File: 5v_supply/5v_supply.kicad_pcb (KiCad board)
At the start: 2 copper layers, 32 x 26 mm, 20 parts, among them J1 B2B-XH-A, J2 BM3B-GHS, J3 B2B-XH-A, U1 LM2678SX-5.0

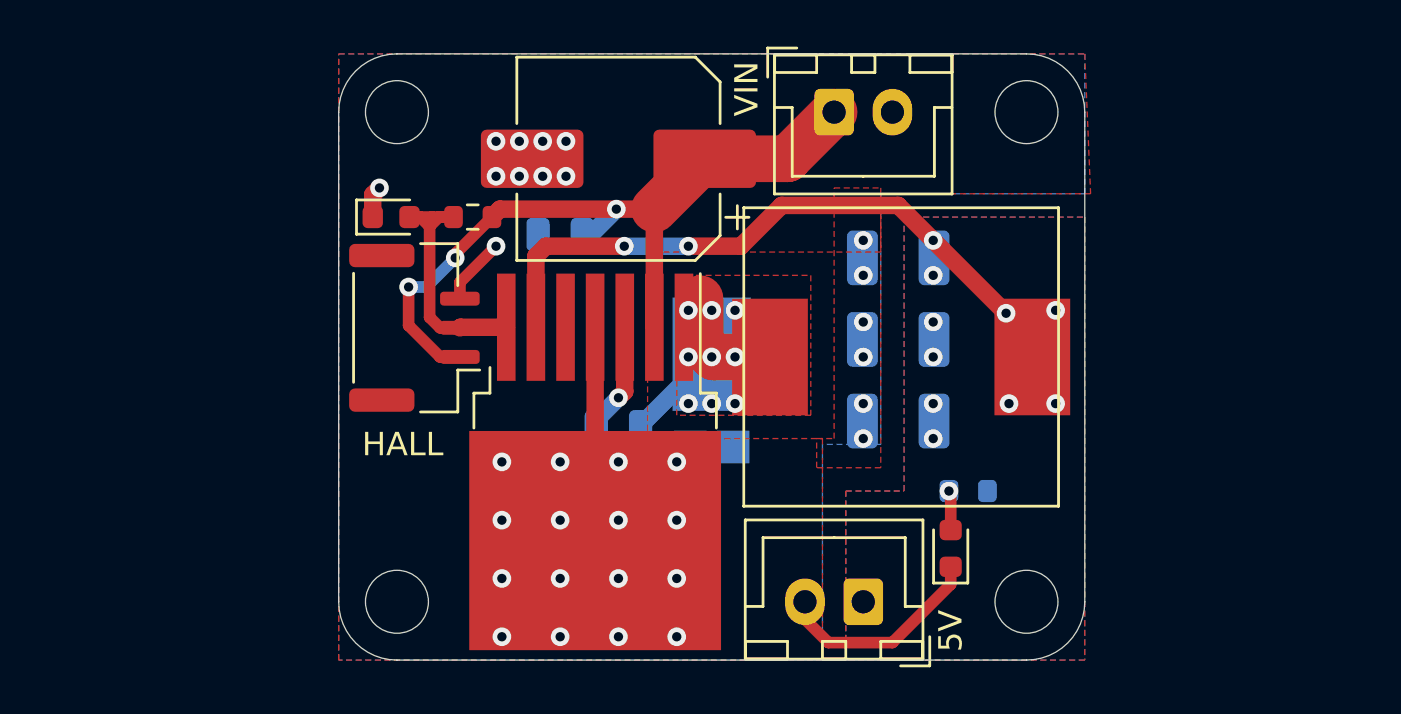
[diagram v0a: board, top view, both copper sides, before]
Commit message: changed layout to a more wide format
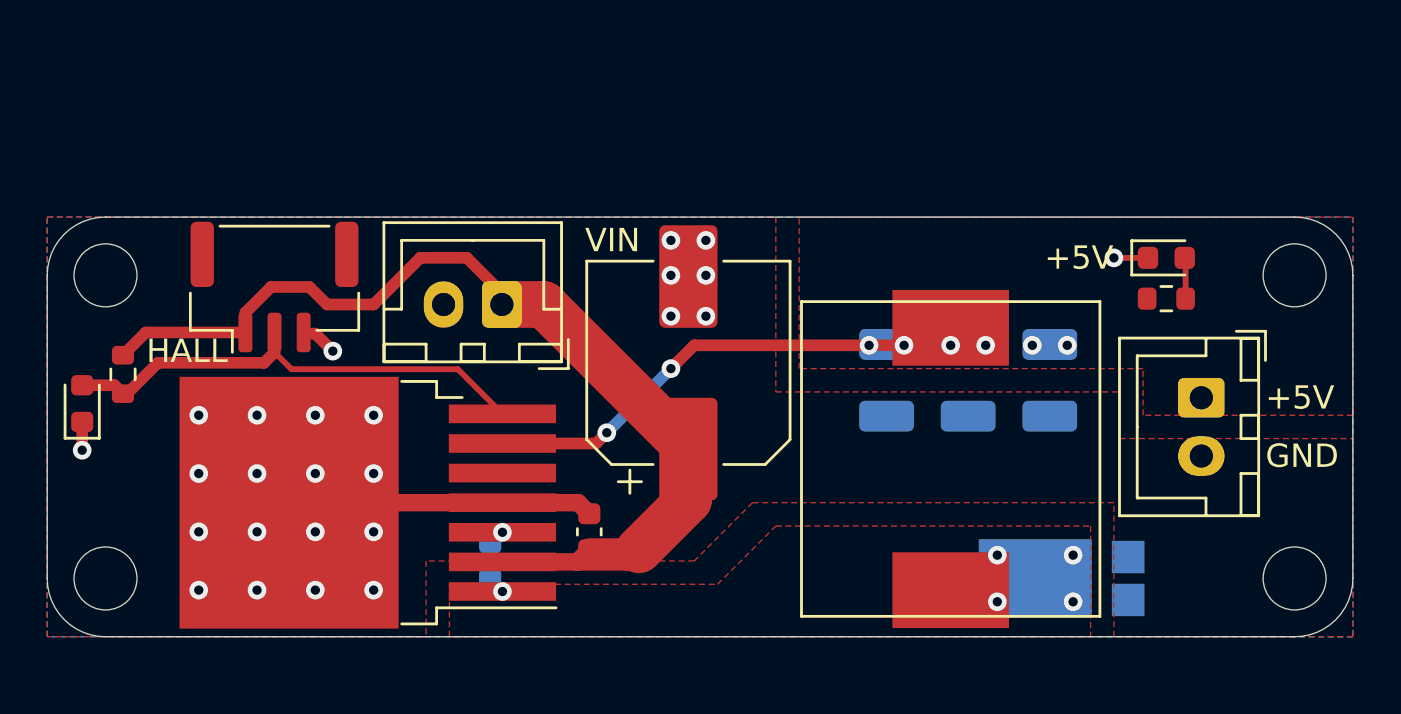
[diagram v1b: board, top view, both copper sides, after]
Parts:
- C2: footprint Capacitor_SMD:C_0805_2012Metric -> Capacitor_SMD:C_0603_1608Metric; moved to F.Cu
- C3: footprint Capacitor_SMD:C_0805_2012Metric -> Capacitor_SMD:C_0603_1608Metric
- R3: moved to F.Cu
- moved D1 17.2 mm to (69.0, 42.5), turned to 0 degrees
- moved J3 16.9 mm to (75.0, 34.8), turned to 270 degrees
- moved J1 16.5 mm to (45.0, 30.8), turned to 180 degrees
- moved R1 16.4 mm to (28.8, 33.8), turned to 270 degrees
- moved D4 15.5 mm to (73.5, 28.8), turned to 0 degrees
- moved D2 15.5 mm to (27.0, 35.0), turned to 90 degrees
- moved H4 14.3 mm to (28.0, 29.5)
- moved H3 13.5 mm to (79.0, 29.5)
- moved C2 12.8 mm to (48.8, 40.5), turned to 90 degrees
- moved L1 12.7 mm to (64.2, 43.0), turned to 90 degrees
- moved H1 12.5 mm to (28.0, 42.5)
- moved R3 11.8 mm to (73.5, 30.5), turned to 0 degrees
- moved H2 11.5 mm to (79.0, 42.5)
- moved U1 9.91 mm to (39.2, 39.2), turned to 180 degrees
- moved C1 9.25 mm to (53.0, 33.2), turned to 90 degrees
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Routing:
- net /+BATT: track 32.8 -> 44.6 mm, vias 3 -> 0
- net /HALL_OUT: track 11.9 -> 20.9 mm
- net /SWITCH: track 9.54 -> 0.82 mm, vias 9 -> 5
- net +5V: track 28.4 -> 21.3 mm, vias 12 -> 8
- net GND: track 22.6 -> 17.4 mm, vias 32 -> 25
- net Net-(C3-Pad2): track 4.78 -> 0.71 mm
- net Net-(D4-Pad2): track 1.71 -> 1.77 mm, vias 1 -> 0
- removed copper zone on B.Cu, net +5V
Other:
- board size 32 x 26 mm -> 56 x 18 mm
- board text added: "+5V"
- board text added: "GND"
- board text added: "v1.1"
- board text removed: "5V"
- board text removed: "v1.0"

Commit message: replaced hall connector with pads
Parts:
- removed J2: BM3B-GHS, Connector_JST:JST_GH_BM03B-GHS-TBT_1x03-1MP_P1.25mm_Vertical
- added TP1: TestPoint, TestPoint:TestPoint_THTPad_D1.5mm_Drill0.7mm, F.Cu at (32.5, 28.8)
- added TP2: TestPoint, TestPoint:TestPoint_THTPad_D1.5mm_Drill0.7mm, F.Cu at (35.2, 28.8)
- added TP3: TestPoint, TestPoint:TestPoint_THTPad_D1.5mm_Drill0.7mm, F.Cu at (38.0, 28.8)
- C1: footprint Capacitor_SMD:CP_Elec_8x10.5 -> Capacitor_SMD:CP_Elec_8x11.9
- moved D2 11.1 mm to (37.8, 32.2), turned to 180 degrees
- moved R1 4.51 mm to (33.0, 32.2), turned to 0 degrees
- moved C1 0.25 mm to (53.0, 33.0)
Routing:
- net /HALL_OUT: track 20.9 -> 17.0 mm
- net GND: track 17.4 -> 14.5 mm, vias 25 -> 20
- net /+BATT: track 44.6 -> 44.4 mm, vias 0 -> 2
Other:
- board text added: "SIG"
- board text added: "V+"
- board text added: "v1.2"
- board text removed: "v1.1"

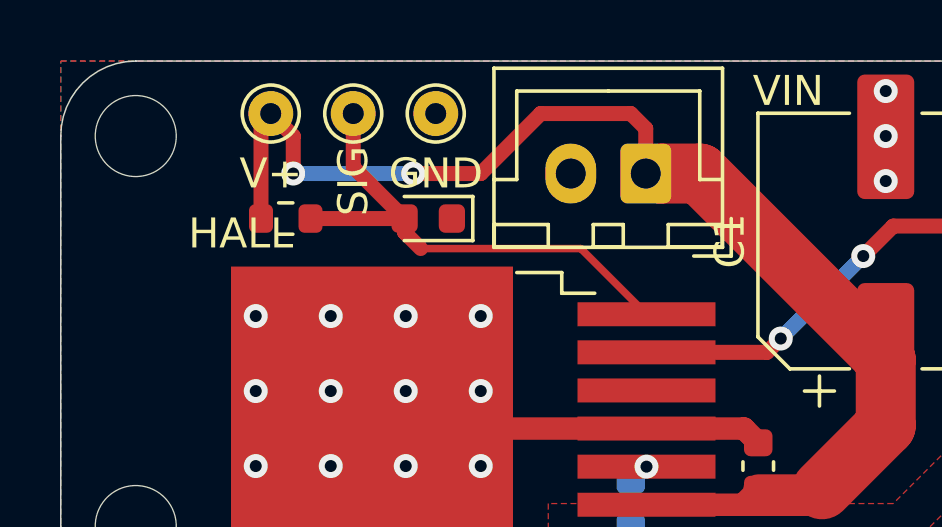
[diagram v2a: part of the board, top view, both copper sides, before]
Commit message: added pcb for power connections of the motors
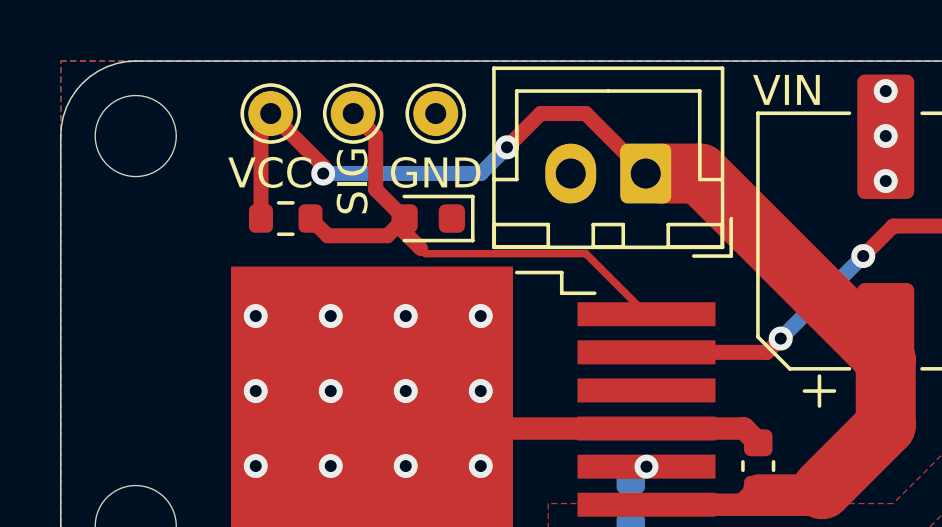
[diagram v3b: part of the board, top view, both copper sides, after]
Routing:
- net /+BATT: track 44.4 -> 43.0 mm
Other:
- board text added: "VCC"
- board text removed: "HALL"
- board text removed: "V+"
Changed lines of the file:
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@@
   (general
     (thickness 1.6)
-    (drawings 22)
-    (tracks 79)
+    (drawings 21)
+    (tracks 82)
     (zones 0)
     (modules 22)
@@
     (tags "capacitor electrolytic")
     (attr smd)
-    (fp_text reference C1 (at 0 -5.2 90) (layer F.SilkS)
+    (fp_text reference C1 (at 0 -5.2 90) (layer F.SilkS) hide
       (effects (font (size 1 1) (thickness 0.15)))
     )
@@
     (effects (font (size 1 1) (thickness 0.15)))
   )
-  (gr_text V+ (at 32.5 30.75) (layer F.SilkS)
+  (gr_text VCC (at 32.5 30.75) (layer F.SilkS)
     (effects (font (size 1 1) (thickness 0.15)))
   )
@@
   (gr_line (start 81.5 29.5) (end 81.5 42.5) (layer Edge.Cuts) (width 0.05))
   (gr_line (start 28 27) (end 79 27) (layer Edge.Cuts) (width 0.05))
-  (gr_text HALL (at 31.5 32.75) (layer F.SilkS)
-    (effects (font (size 1 1) (thickness 0.15)))
-  )
   (gr_text VIN (at 49.75 28) (layer F.SilkS)
     (effects (font (size 1 1) (thickness 0.15)))
@@
   (segment (start 32.175 29.075) (end 32.5 28.75) (width 0.5) (layer F.Cu) (net 1))
   (segment (start 32.175 32.25) (end 32.175 29.075) (width 0.5) (layer F.Cu) (net 1))
-  (segment (start 45 30.75) (end 45 29.25) (width 0.5) (layer F.Cu) (net 1))
-  (segment (start 45 29.25) (end 44.5 28.75) (width 0.5) (layer F.Cu) (net 1))
-  (segment (start 44.5 28.75) (end 41.5 28.75) (width 0.5) (layer F.Cu) (net 1))
-  (segment (start 41.5 28.75) (end 39.5 30.75) (width 0.5) (layer F.Cu) (net 1))
-  (via (at 37.25 30.75) (size 0.8) (drill 0.4) (layers F.Cu B.Cu) (net 1))
-  (segment (start 39.5 30.75) (end 37.25 30.75) (width 0.5) (layer F.Cu) (net 1))
-  (via (at 33.25 30.75) (size 0.8) (drill 0.4) (layers F.Cu B.Cu) (net 1))
-  (segment (start 37.25 30.75) (end 33.25 30.75) (width 0.5) (layer B.Cu) (net 1))
-  (segment (start 32.5 28.75) (end 33.25 29.5) (width 0.5) (layer F.Cu) (net 1))
-  (segment (start 33.25 29.5) (end 33.25 30.75) (width 0.5) (layer F.Cu) (net 1))
+  (via (at 34.24998 30.75) (size 0.8) (drill 0.4) (layers F.Cu B.Cu) (net 1))
+  (segment (start 34.24998 30.49998) (end 34.24998 30.75) (width 0.5) (layer F.Cu) (net 1))
+  (segment (start 32.5 28.75) (end 34.24998 30.49998) (width 0.5) (layer F.Cu) (net 1))
+  (segment (start 45 30.75) (end 43 28.75) (width 0.5) (layer F.Cu) (net 1))
+  (segment (start 39.5 30.75) (end 40.375 29.875) (width 0.5) (layer B.Cu) (net 1))
+  (segment (start 43 28.75) (end 41.5 28.75) (width 0.5) (layer F.Cu) (net 1))
+  (segment (start 34.24998 30.75) (end 39.5 30.75) (width 0.5) (layer B.Cu) (net 1))
+  (segment (start 41.5 28.75) (end 40.375 29.875) (width 0.5) (layer F.Cu) (net 1))
+  (via (at 40.375 29.875) (size 0.8) (drill 0.4) (layers F.Cu B.Cu) (net 1))
   (via (at 39.5 43) (size 0.8) (drill 0.4) (layers F.Cu B.Cu) (net 2))
   (via (at 39.5 40.5) (size 0.8) (drill 0.4) (layers F.Cu B.Cu) (net 2))
@@
   (segment (start 53.25 32.5) (end 63.5 32.5) (width 0.5) (layer F.Cu) (net 4))
   (segment (start 52.25 33.5) (end 53.25 32.5) (width 0.5) (layer F.Cu) (net 4))
-  (segment (start 35.25 30.5375) (end 36.9625 32.25) (width 0.5) (layer F.Cu) (net 5))
-  (segment (start 35.25 28.75) (end 35.25 30.5375) (width 0.5) (layer F.Cu) (net 5))
-  (segment (start 42.835 33.25) (end 45.025 35.44) (width 0.25) (layer F.Cu) (net 5))
-  (segment (start 37.5 33.25) (end 42.835 33.25) (width 0.25) (layer F.Cu) (net 5))
   (segment (start 36.9625 32.7125) (end 37.5 33.25) (width 0.5) (layer F.Cu) (net 5))
   (segment (start 36.9625 32.25) (end 36.9625 32.7125) (width 0.5) (layer F.Cu) (net 5))
-  (segment (start 36.9625 32.25) (end 33.825 32.25) (width 0.5) (layer F.Cu) (net 5))
+  (segment (start 35.999999 31.287499) (end 36.9625 32.25) (width 0.5) (layer F.Cu) (net 5))
+  (segment (start 36.9625 32.25) (end 36.389162 32.823338) (width 0.5) (layer F.Cu) (net 5))
+  (segment (start 36.389162 32.823338) (end 34.398338 32.823338) (width 0.5) (layer F.Cu) (net 5))
+  (segment (start 34.398338 32.823338) (end 33.825 32.25) (width 0.5) (layer F.Cu) (net 5))
+  (segment (start 35.25 28.75) (end 35.999999 29.499999) (width 0.5) (layer F.Cu) (net 5))
+  (segment (start 35.999999 29.499999) (end 35.999999 31.287499) (width 0.5) (layer F.Cu) (net 5))
+  (segment (start 43.005379 33.420379) (end 45.025 35.44) (width 0.25) (layer F.Cu) (net 5))
+  (segment (start 37.670379 33.420379) (end 43.005379 33.420379) (width 0.25) (layer F.Cu) (net 5))
+  (segment (start 37.5 33.25) (end 37.670379 33.420379) (width 0.25) (layer F.Cu) (net 5))
   (via (at 69.5 43.5) (size 0.8) (drill 0.4) (layers F.Cu B.Cu) (net 7))
   (via (at 66.25 43.5) (size 0.8) (drill 0.4) (layers F.Cu B.Cu) (net 7))
